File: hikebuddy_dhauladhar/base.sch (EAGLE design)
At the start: 116 parts, among them J1 MF-CON-MICROUSB-RIGHT, J2 GPS Port, J5 SOLDER_PAD_2, U1 LTC3586EUFE-1#PBF, U2 MAX17260SETD+, U3 MF-DSC-SOT233-MMBT3904, U4 MF-DSC-SOT233-MMBT3904, U5 DRV2605LTDGSRQ1, U6 BMX160

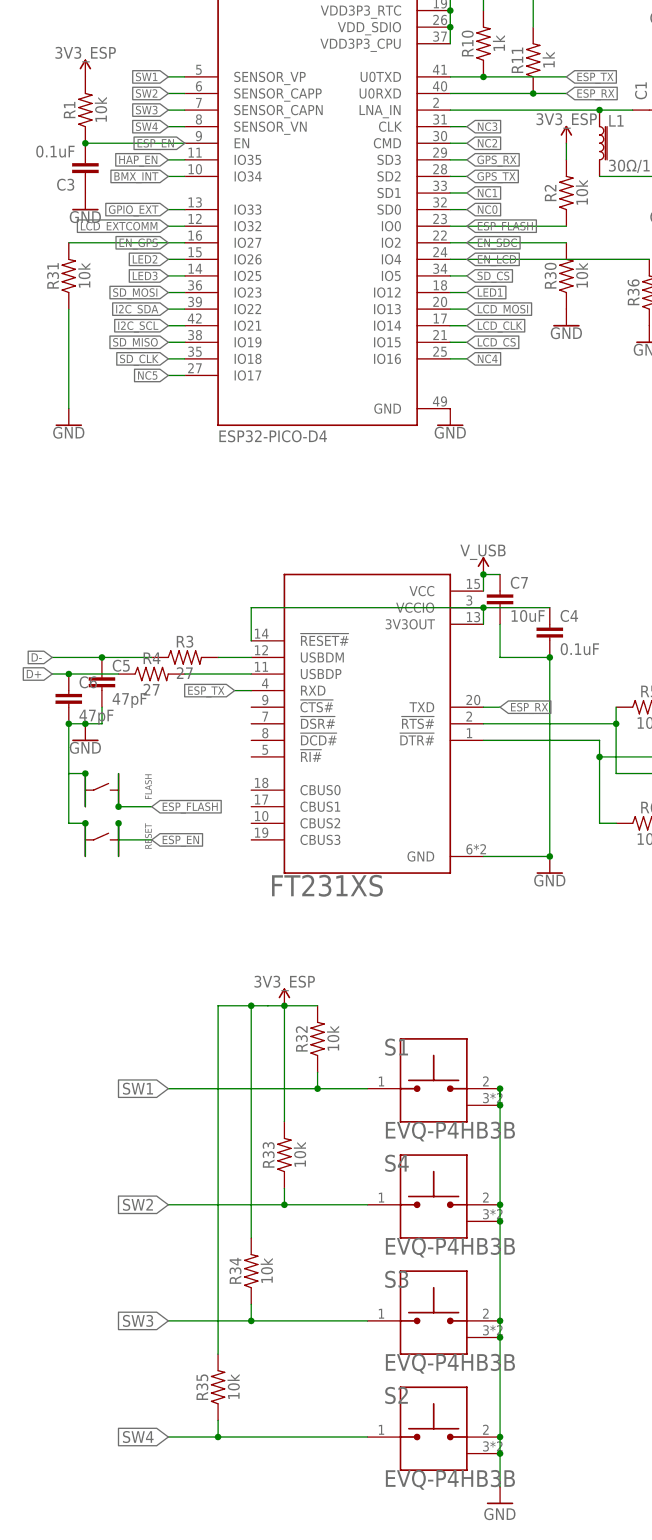
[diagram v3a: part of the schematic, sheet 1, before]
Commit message: export cam files
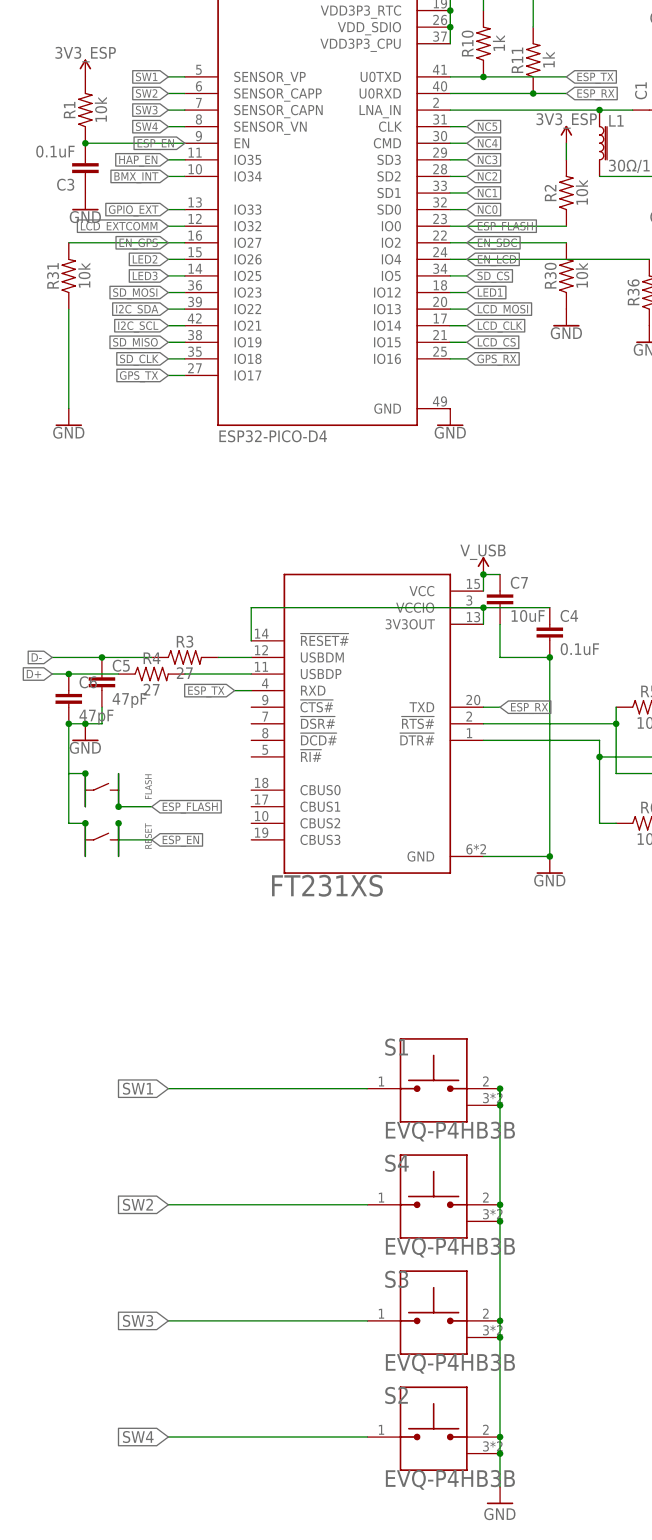
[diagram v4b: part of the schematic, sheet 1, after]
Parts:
- removed R32, R33, R34, R35: 10k, SparkFun-Resistors:10KOHM-0603-1/10W-1%
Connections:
- net GPS_RX: now also ESP32-PICO-D4.IO16; no longer ESP32-PICO-D4.SD3
- net GPS_TX: now also ESP32-PICO-D4.IO17; no longer ESP32-PICO-D4.SD2
- net NC2: now also ESP32-PICO-D4.SD2; no longer ESP32-PICO-D4.CMD
- net NC3: now also ESP32-PICO-D4.SD3; no longer ESP32-PICO-D4.CLK
- net NC4: now also ESP32-PICO-D4.CMD; no longer ESP32-PICO-D4.IO16
- net NC5: now also ESP32-PICO-D4.CLK; no longer ESP32-PICO-D4.IO17
- net SW1: no longer R32.1
- net SW2: no longer R33.1
- net SW3: no longer R34.1
- net SW4: no longer R35.1
- net VCC: no longer R32.2, R33.2, R34.2, R35.2
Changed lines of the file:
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@@
 <part name="C37" library="SparkFun-Capacitors" deviceset="4.7UF" device="-0603-6.3V-(10%)" package3d_urn="urn:adsk.eagle:package:23616/2" value="4.7uF"/>
 <part name="GND14" library="supply1" library_urn="urn:adsk.eagle:library:371" deviceset="GND" device=""/>
-<part name="R32" library="SparkFun-Resistors" deviceset="10KOHM" device="-0603-1/10W-1%" package3d_urn="urn:adsk.eagle:package:23555/3" value="10k"/>
-<part name="R33" library="SparkFun-Resistors" deviceset="10KOHM" device="-0603-1/10W-1%" package3d_urn="urn:adsk.eagle:package:23555/3" value="10k"/>
-<part name="R34" library="SparkFun-Resistors" deviceset="10KOHM" device="-0603-1/10W-1%" package3d_urn="urn:adsk.eagle:package:23555/3" value="10k"/>
-<part name="R35" library="SparkFun-Resistors" deviceset="10KOHM" device="-0603-1/10W-1%" package3d_urn="urn:adsk.eagle:package:23555/3" value="10k"/>
 <part name="GND15" library="SparkFun-PowerSymbols" library_urn="urn:adsk.eagle:library:530" deviceset="GND" device=""/>
-<part name="3V3_ESP3" library="SparkFun-PowerSymbols" library_urn="urn:adsk.eagle:library:530" deviceset="VCC" device="" value="3V3_ESP"/>
 <part name="R30" library="SparkFun-Resistors" deviceset="10KOHM" device="-0603-1/10W-1%" package3d_urn="urn:adsk.eagle:package:23555/3" value="10k"/>
 <part name="GND16" library="SparkFun-PowerSymbols" library_urn="urn:adsk.eagle:library:530" deviceset="GND" device=""/>
@@
 <attribute name="VALUE" x="76.2" y="-43.18" size="1.778" layer="96"/>
 </instance>
-<instance part="R32" gate="G$1" x="50.8" y="30.48" smashed="yes" rot="R90">
-<attribute name="NAME" x="49.276" y="30.48" size="1.778" layer="95" font="vector" rot="R90" align="bottom-center"/>
-<attribute name="VALUE" x="52.324" y="30.48" size="1.778" layer="96" font="vector" rot="R90" align="top-center"/>
-</instance>
-<instance part="R33" gate="G$1" x="45.72" y="12.7" smashed="yes" rot="R90">
-<attribute name="NAME" x="44.196" y="12.7" size="1.778" layer="95" font="vector" rot="R90" align="bottom-center"/>
-<attribute name="VALUE" x="47.244" y="12.7" size="1.778" layer="96" font="vector" rot="R90" align="top-center"/>
-</instance>
-<instance part="R34" gate="G$1" x="40.64" y="-5.08" smashed="yes" rot="R90">
-<attribute name="NAME" x="39.116" y="-5.08" size="1.778" layer="95" font="vector" rot="R90" align="bottom-center"/>
-<attribute name="VALUE" x="42.164" y="-5.08" size="1.778" layer="96" font="vector" rot="R90" align="top-center"/>
-</instance>
-<instance part="R35" gate="G$1" x="35.56" y="-22.86" smashed="yes" rot="R90">
-<attribute name="NAME" x="34.036" y="-22.86" size="1.778" layer="95" font="vector" rot="R90" align="bottom-center"/>
-<attribute name="VALUE" x="37.084" y="-22.86" size="1.778" layer="96" font="vector" rot="R90" align="top-center"/>
-</instance>
-<instance part="3V3_ESP3" gate="G$1" x="45.72" y="35.56" smashed="yes">
-<attribute name="VALUE" x="45.72" y="38.354" size="1.778" layer="96" align="bottom-center"/>
-</instance>
 <instance part="R30" gate="G$1" x="88.9" y="147.32" smashed="yes" rot="R90">
 <attribute name="NAME" x="87.376" y="147.32" size="1.778" layer="95" font="vector" rot="R90" align="bottom-center"/>
@@
 <pinref part="D4" gate="G$1" pin="ANODE"/>
 <pinref part="3V3_ESP13" gate="G$1" pin="VCC"/>
-</segment>
-<segment>
-<pinref part="R35" gate="G$1" pin="2"/>
-<pinref part="R32" gate="G$1" pin="2"/>
-<wire x1="35.56" y1="-17.78" x2="35.56" y2="35.56" width="0.1524" layer="91"/>
-<wire x1="35.56" y1="35.56" x2="40.64" y2="35.56" width="0.1524" layer="91"/>
-<pinref part="R34" gate="G$1" pin="2"/>
-<wire x1="40.64" y1="35.56" x2="43.18" y2="35.56" width="0.1524" layer="91"/>
-<wire x1="45.72" y1="35.56" x2="50.8" y2="35.56" width="0.1524" layer="91"/>
-<wire x1="40.64" y1="0" x2="40.64" y2="35.56" width="0.1524" layer="91"/>
-<junction x="40.64" y="35.56"/>
-<pinref part="R33" gate="G$1" pin="2"/>
-<wire x1="45.72" y1="17.78" x2="45.72" y2="35.56" width="0.1524" layer="91"/>
-<wire x1="45.72" y1="35.56" x2="43.18" y2="35.56" width="0.1524" layer="91"/>
-<pinref part="3V3_ESP3" gate="G$1" pin="VCC"/>
-<junction x="45.72" y="35.56"/>
 </segment>
 <segment>
@@
 <net name="NC2" class="0">
 <segment>
-<pinref part="ESP32-PICO-D4" gate="G$1" pin="CMD"/>
-<wire x1="71.12" y1="167.64" x2="73.66" y2="167.64" width="0.1524" layer="91"/>
-<label x="73.66" y="167.64" size="1.27" layer="95" xref="yes"/>
+<pinref part="ESP32-PICO-D4" gate="G$1" pin="SD2"/>
+<wire x1="71.12" y1="162.56" x2="73.66" y2="162.56" width="0.1524" layer="91"/>
+<label x="73.66" y="162.56" size="1.27" layer="95" xref="yes"/>
 </segment>
 </net>
 <net name="NC3" class="0">
 <segment>
-<pinref part="ESP32-PICO-D4" gate="G$1" pin="CLK"/>
-<wire x1="71.12" y1="170.18" x2="73.66" y2="170.18" width="0.1524" layer="91"/>
-<label x="73.66" y="170.18" size="1.27" layer="95" xref="yes"/>
+<pinref part="ESP32-PICO-D4" gate="G$1" pin="SD3"/>
+<wire x1="71.12" y1="165.1" x2="73.66" y2="165.1" width="0.1524" layer="91"/>
+<label x="73.66" y="165.1" size="1.27" layer="95" xref="yes"/>
 </segment>
 </net>
@@
 <wire x1="71.12" y1="160.02" x2="73.66" y2="160.02" width="0.1524" layer="91"/>
 <label x="73.66" y="160.02" size="1.27" layer="95" xref="yes"/>
-</segment>
-</net>
-<net name="NC4" class="0">
-<segment>
-<pinref part="ESP32-PICO-D4" gate="G$1" pin="IO16"/>
-<wire x1="71.12" y1="134.62" x2="73.66" y2="134.62" width="0.1524" layer="91"/>
-<label x="73.66" y="134.62" size="1.27" layer="95" xref="yes"/>
-</segment>
-</net>
-<net name="NC5" class="0">
-<segment>
-<pinref part="ESP32-PICO-D4" gate="G$1" pin="IO17"/>
-<wire x1="30.48" y1="132.08" x2="27.94" y2="132.08" width="0.1524" layer="91"/>
-<label x="27.94" y="132.08" size="1.27" layer="95" rot="R180" xref="yes"/>
 </segment>
 </net>
@@
 </segment>
 <segment>
-<pinref part="ESP32-PICO-D4" gate="G$1" pin="SD3"/>
-<wire x1="71.12" y1="165.1" x2="73.66" y2="165.1" width="0.1524" layer="91"/>
-<label x="73.66" y="165.1" size="1.27" layer="95" xref="yes"/>
+<pinref part="ESP32-PICO-D4" gate="G$1" pin="IO16"/>
+<wire x1="71.12" y1="134.62" x2="73.66" y2="134.62" width="0.1524" layer="91"/>
+<label x="73.66" y="134.62" size="1.27" layer="95" xref="yes"/>
 </segment>
 </net>
@@
 </segment>
 <segment>
-<pinref part="ESP32-PICO-D4" gate="G$1" pin="SD2"/>
-<wire x1="71.12" y1="162.56" x2="73.66" y2="162.56" width="0.1524" layer="91"/>
-<label x="73.66" y="162.56" size="1.27" layer="95" xref="yes"/>
+<pinref part="ESP32-PICO-D4" gate="G$1" pin="IO17"/>
+<wire x1="30.48" y1="132.08" x2="27.94" y2="132.08" width="0.1524" layer="91"/>
+<label x="27.94" y="132.08" size="1.27" layer="95" rot="R180" xref="yes"/>
 </segment>
 </net>
@@
 <net name="SW1" class="0">
 <segment>
-<pinref part="R32" gate="G$1" pin="1"/>
-<wire x1="58.42" y1="22.86" x2="50.8" y2="22.86" width="0.1524" layer="91"/>
-<wire x1="50.8" y1="22.86" x2="50.8" y2="25.4" width="0.1524" layer="91"/>
-<wire x1="50.8" y1="22.86" x2="27.94" y2="22.86" width="0.1524" layer="91"/>
-<junction x="50.8" y="22.86"/>
+<wire x1="58.42" y1="22.86" x2="27.94" y2="22.86" width="0.1524" layer="91"/>
 <label x="27.94" y="22.86" size="1.778" layer="95" rot="R180" xref="yes"/>
 <pinref part="S1" gate="G$1" pin="1"/>
@@
 <net name="SW2" class="0">
 <segment>
-<pinref part="R33" gate="G$1" pin="1"/>
-<wire x1="58.42" y1="5.08" x2="45.72" y2="5.08" width="0.1524" layer="91"/>
-<wire x1="45.72" y1="5.08" x2="45.72" y2="7.62" width="0.1524" layer="91"/>
-<wire x1="45.72" y1="5.08" x2="27.94" y2="5.08" width="0.1524" layer="91"/>
-<junction x="45.72" y="5.08"/>
+<wire x1="58.42" y1="5.08" x2="27.94" y2="5.08" width="0.1524" layer="91"/>
 <label x="27.94" y="5.08" size="1.778" layer="95" rot="R180" xref="yes"/>
 <pinref part="S4" gate="G$1" pin="1"/>
@@
 <net name="SW3" class="0">
 <segment>
-<pinref part="R34" gate="G$1" pin="1"/>
-<wire x1="58.42" y1="-12.7" x2="40.64" y2="-12.7" width="0.1524" layer="91"/>
-<wire x1="40.64" y1="-12.7" x2="40.64" y2="-10.16" width="0.1524" layer="91"/>
-<wire x1="40.64" y1="-12.7" x2="27.94" y2="-12.7" width="0.1524" layer="91"/>
-<junction x="40.64" y="-12.7"/>
+<wire x1="58.42" y1="-12.7" x2="27.94" y2="-12.7" width="0.1524" layer="91"/>
 <label x="27.94" y="-12.7" size="1.778" layer="95" rot="R180" xref="yes"/>
 <pinref part="S3" gate="G$1" pin="1"/>
@@
 <net name="SW4" class="0">
 <segment>
-<pinref part="R35" gate="G$1" pin="1"/>
-<wire x1="58.42" y1="-30.48" x2="35.56" y2="-30.48" width="0.1524" layer="91"/>
-<wire x1="35.56" y1="-30.48" x2="35.56" y2="-27.94" width="0.1524" layer="91"/>
-<wire x1="35.56" y1="-30.48" x2="27.94" y2="-30.48" width="0.1524" layer="91"/>
-<junction x="35.56" y="-30.48"/>
+<wire x1="58.42" y1="-30.48" x2="27.94" y2="-30.48" width="0.1524" layer="91"/>
 <label x="27.94" y="-30.48" size="1.778" layer="95" rot="R180" xref="yes"/>
 <pinref part="S2" gate="G$1" pin="1"/>
@@
 </segment>
 </net>
+<net name="NC4" class="0">
+<segment>
+<pinref part="ESP32-PICO-D4" gate="G$1" pin="CMD"/>
+<wire x1="71.12" y1="167.64" x2="73.66" y2="167.64" width="0.1524" layer="91"/>
+<label x="73.66" y="167.64" size="1.27" layer="95" xref="yes"/>
+</segment>
+</net>
+<net name="NC5" class="0">
+<segment>
+<pinref part="ESP32-PICO-D4" gate="G$1" pin="CLK"/>
+<wire x1="71.12" y1="170.18" x2="73.66" y2="170.18" width="0.1524" layer="91"/>
+<label x="73.66" y="170.18" size="1.27" layer="95" xref="yes"/>
+</segment>
+</net>

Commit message: rerouted traces close to milling; moved milling layer to dimension
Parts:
- BATTERY1: value (none) -> S2B-PH-SM4-TB(LF)(SN); SPICEPREFIX (none) -> E
- C14, C15: device SparkFun-Capacitors:0.1UF-0603-25V-5% -> SparkFun-Capacitors:0.1UF-0603-25V-(+80/-20%)
- C9: device MF_Passives:CAPACITOR_NP_1206 -> MF_Passives:CAPACITOR_NP_0603
- J2, J3, J4, J6, J7, J8: DNP (none) -> 1
- U1: MP (none) -> LTC3586EUFE
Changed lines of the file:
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@@
 <part name="R13" library="SparkFun-Resistors" deviceset="10KOHM" device="-0603-1/10W-1%" package3d_urn="urn:adsk.eagle:package:23555/3" value="10k"/>
 <part name="R14" library="SparkFun-Resistors" deviceset="10KOHM" device="-0603-1/10W-1%" package3d_urn="urn:adsk.eagle:package:23555/3" value="10k"/>
-<part name="C14" library="SparkFun-Capacitors" deviceset="0.1UF" device="-0603-25V-5%" package3d_urn="urn:adsk.eagle:package:23616/2" value="0.1uF"/>
-<part name="C15" library="SparkFun-Capacitors" deviceset="0.1UF" device="-0603-25V-5%" package3d_urn="urn:adsk.eagle:package:23616/2" value="0.1uF"/>
+<part name="C14" library="SparkFun-Capacitors" deviceset="0.1UF" device="-0603-25V-(+80/-20%)" package3d_urn="urn:adsk.eagle:package:23616/2" value="0.1uF"/>
+<part name="C15" library="SparkFun-Capacitors" deviceset="0.1UF" device="-0603-25V-(+80/-20%)" package3d_urn="urn:adsk.eagle:package:23616/2" value="0.1uF"/>
 <part name="GND13" library="supply1" library_urn="urn:adsk.eagle:library:371" deviceset="GND" device=""/>
 <part name="GND26" library="supply1" library_urn="urn:adsk.eagle:library:371" deviceset="GND" device=""/>
@@
 <attribute name="DNP" value="1"/>
 </part>
-<part name="J2" library="SparkFun-Connectors" deviceset="CONN_06" device="LOCK" value="GPS Port"/>
+<part name="J2" library="SparkFun-Connectors" deviceset="CONN_06" device="LOCK" value="GPS Port">
+<attribute name="DNP" value="1"/>
+</part>
 <part name="GND9" library="supply1" library_urn="urn:adsk.eagle:library:371" deviceset="GND" device=""/>
-<part name="U1" library="LTC3586EUFE-3_TRPBF" deviceset="LTC3586EUFE-3#TRPBF" device="" package3d_urn="urn:adsk.eagle:package:16348004/2" value=" LTC3586EUFE-1#PBF"/>
+<part name="U1" library="LTC3586EUFE-3_TRPBF" deviceset="LTC3586EUFE-3#TRPBF" device="" package3d_urn="urn:adsk.eagle:package:16348004/2" value=" LTC3586EUFE-1#PBF">
+<attribute name="MP" value="LTC3586EUFE"/>
+</part>
 <part name="U2" library="MAX17260SETD_coulomb" deviceset="MAX17260SETD+" device="" package3d_urn="urn:adsk.eagle:package:16348021/2"/>
-<part name="BATTERY1" library="SparkFun-Connectors" deviceset="JST_2MM_MALE" device="" override_package3d_urn="urn:adsk.eagle:package:16346146/2" override_package_urn="urn:adsk.eagle:footprint:16346147/1"/>
+<part name="BATTERY1" library="SparkFun-Connectors" deviceset="JST_2MM_MALE" device="" override_package3d_urn="urn:adsk.eagle:package:16346146/2" override_package_urn="urn:adsk.eagle:footprint:16346147/1" value="S2B-PH-SM4-TB(LF)(SN)">
+<attribute name="SPICEPREFIX" value="E"/>
+</part>
 <part name="SUPPLY2" library="SparkFun-PowerSymbols" library_urn="urn:adsk.eagle:library:530" deviceset="V_USB" device=""/>
 <part name="J1" library="MF_Connectors" deviceset="USB" device="_MICRO_RIGHT" package3d_urn="urn:adsk.eagle:package:9948223/2" value="MF-CON-MICROUSB-RIGHT"/>
 <part name="GND7" library="SparkFun-PowerSymbols" library_urn="urn:adsk.eagle:library:530" deviceset="GND" device=""/>
-<part name="C9" library="MF_Passives" deviceset="CAPACITOR_NP" device="_1206" package3d_urn="urn:adsk.eagle:package:16347921/2" value="10uF"/>
+<part name="C9" library="MF_Passives" library_urn="urn:adsk.eagle:library:16347882" deviceset="CAPACITOR_NP" device="_0603" package3d_urn="urn:adsk.eagle:package:16347923/3" value="10uF"/>
 <part name="GND10" library="SparkFun-PowerSymbols" library_urn="urn:adsk.eagle:library:530" deviceset="GND" device=""/>
 <part name="R7" library="MF_Passives" deviceset="RESISTOR" device="_0603" package3d_urn="urn:adsk.eagle:package:16347927/2" value="2K"/>
@@
 <part name="C19" library="SparkFun-Capacitors" deviceset="4.7UF" device="-0603-6.3V-(10%)" package3d_urn="urn:adsk.eagle:package:23616/2" value="4.7uF"/>
 <part name="GND22" library="supply1" library_urn="urn:adsk.eagle:library:371" deviceset="GND" device=""/>
-<part name="J3" library="SparkFun-Connectors" deviceset="CONN_03" device="LOCK"/>
-<part name="J4" library="SparkFun-Connectors" deviceset="CONN_03" device="LOCK"/>
+<part name="J3" library="SparkFun-Connectors" deviceset="CONN_03" device="LOCK">
+<attribute name="DNP" value="1"/>
+</part>
+<part name="J4" library="SparkFun-Connectors" deviceset="CONN_03" device="LOCK">
+<attribute name="DNP" value="1"/>
+</part>
 <part name="J5" library="SparkFun-Connectors" deviceset="SOLDER_PAD_2" device=""/>
-<part name="J6" library="SparkFun-Connectors" deviceset="CONN_01" device=""/>
-<part name="J7" library="SparkFun-Connectors" deviceset="CONN_01" device=""/>
-<part name="J8" library="SparkFun-Connectors" deviceset="CONN_06" device="LOCK"/>
+<part name="J6" library="SparkFun-Connectors" deviceset="CONN_01" device="">
+<attribute name="DNP" value="1"/>
+</part>
+<part name="J7" library="SparkFun-Connectors" deviceset="CONN_01" device="">
+<attribute name="DNP" value="1"/>
+</part>
+<part name="J8" library="SparkFun-Connectors" deviceset="CONN_06" device="LOCK">
+<attribute name="DNP" value="1"/>
+</part>
 <part name="C8" library="SparkFun-Capacitors" deviceset="4.7PF" device="-0603-50V-5%" package3d_urn="urn:adsk.eagle:package:23616/2" value="10uF"/>
 <part name="C38" library="SparkFun-Capacitors" deviceset="4.7PF" device="-0603-50V-5%" package3d_urn="urn:adsk.eagle:package:23616/2" value="10uF"/>
@@
 <attribute name="VALUE" x="155.194" y="198.12" size="1.778" layer="96" font="vector" rot="R270"/>
 <attribute name="NAME" x="175.768" y="198.12" size="1.778" layer="95" font="vector" rot="R270"/>
+<attribute name="DNP" x="165.1" y="193.04" size="1.778" layer="96" rot="R270" display="off"/>
 </instance>
 <instance part="GND9" gate="1" x="160.02" y="185.42" smashed="yes">
@@
 <attribute name="VALUE" x="134.62" y="20.574" size="1.778" layer="96" font="vector"/>
 <attribute name="NAME" x="134.62" y="33.528" size="1.778" layer="95" font="vector"/>
+<attribute name="DNP" x="137.16" y="27.94" size="1.778" layer="96" display="off"/>
 </instance>
 <instance part="J4" gate="J$1" x="137.16" y="48.26" smashed="yes">
 <attribute name="VALUE" x="134.62" y="40.894" size="1.778" layer="96" font="vector"/>
 <attribute name="NAME" x="134.62" y="53.848" size="1.778" layer="95" font="vector"/>
+<attribute name="DNP" x="137.16" y="48.26" size="1.778" layer="96" display="off"/>
 </instance>
 <instance part="J5" gate="G$1" x="254" y="45.72" smashed="yes" rot="R180">
@@
 <attribute name="VALUE" x="154.94" y="73.914" size="1.778" layer="96" font="vector"/>
 <attribute name="NAME" x="154.94" y="81.788" size="1.778" layer="95" font="vector"/>
+<attribute name="DNP" x="157.48" y="78.74" size="1.778" layer="96" display="off"/>
 </instance>
 <instance part="J7" gate="G$1" x="157.48" y="76.2" smashed="yes">
 <attribute name="VALUE" x="154.94" y="71.374" size="1.778" layer="96" font="vector"/>
 <attribute name="NAME" x="154.94" y="79.248" size="1.778" layer="95" font="vector"/>
+<attribute name="DNP" x="157.48" y="76.2" size="1.778" layer="96" display="off"/>
 </instance>
 <instance part="J8" gate="G$1" x="360.68" y="68.58" smashed="yes" rot="R180">
 <attribute name="VALUE" x="365.76" y="78.486" size="1.778" layer="96" font="vector" rot="R180"/>
 <attribute name="NAME" x="365.76" y="57.912" size="1.778" layer="95" font="vector" rot="R180"/>
+<attribute name="DNP" x="360.68" y="68.58" size="1.778" layer="96" rot="R180" display="off"/>
 </instance>
 <instance part="C8" gate="G$1" x="104.14" y="195.58" smashed="yes" rot="R180">
